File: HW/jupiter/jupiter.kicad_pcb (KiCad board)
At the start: 2 copper layers, 32 parts, among them J1 POWER_IN, J2 Expansion Bus, Q1 DS1813, SW1 RESET, SW2 PANIC, SW3 SPDT, U1 TL7705B, U2 74HC74, U3 DS1511Y+, U4 WD65C816S_PLCC44-65xx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

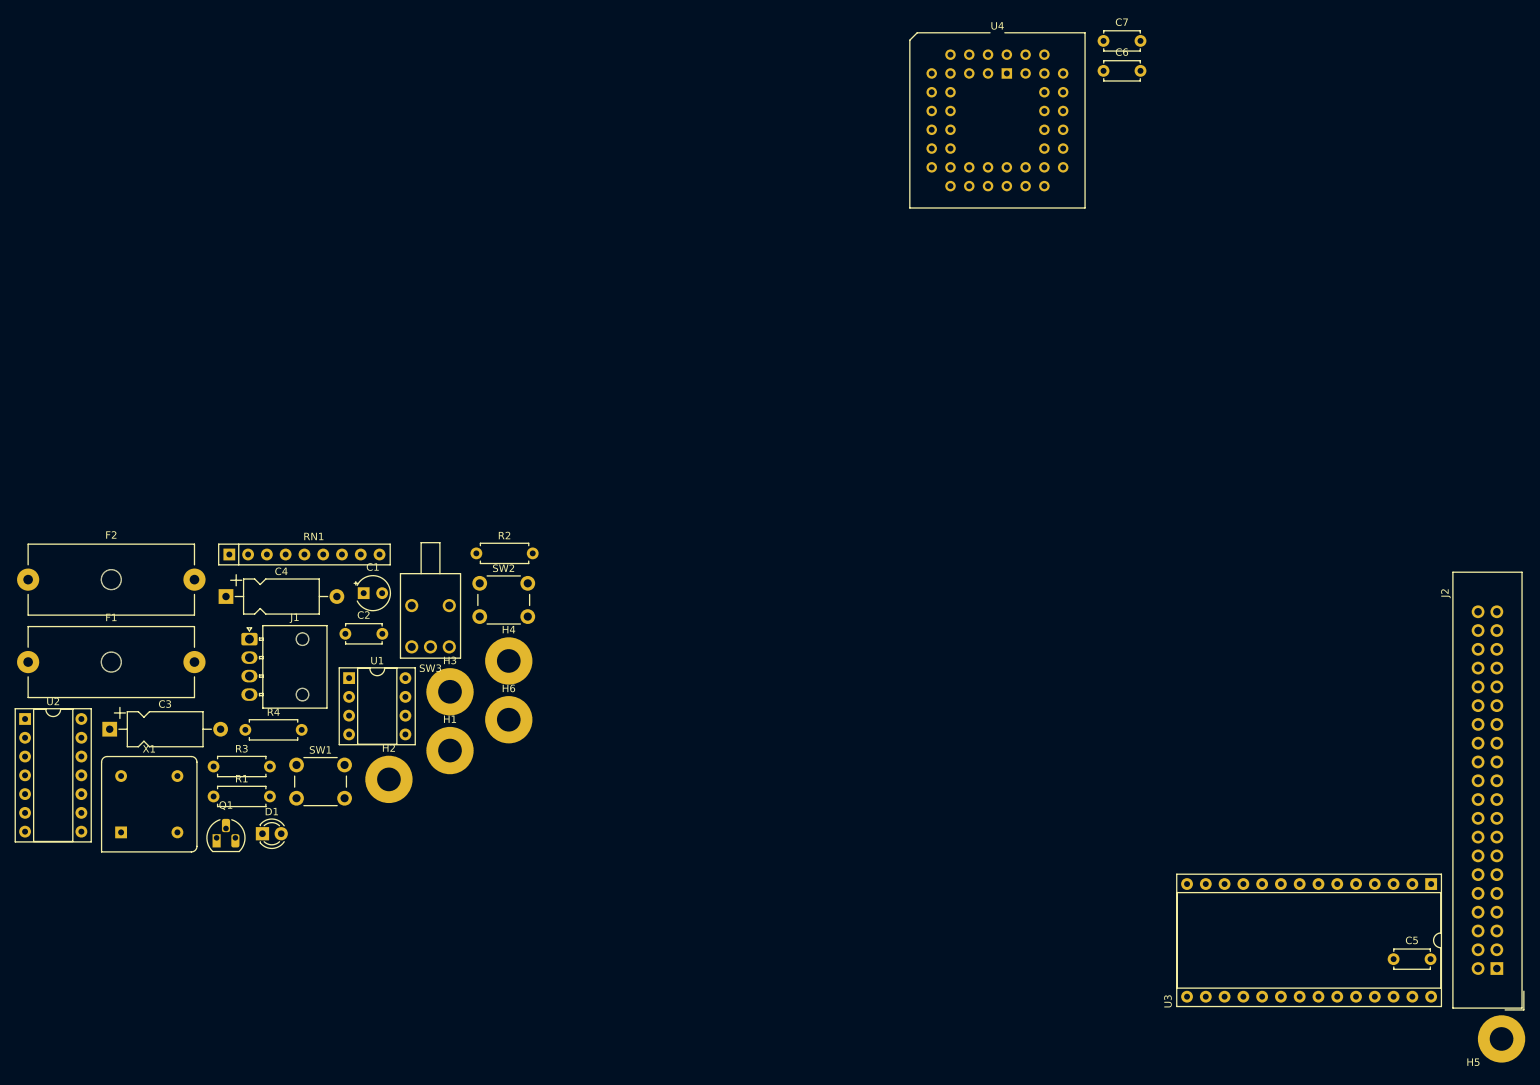
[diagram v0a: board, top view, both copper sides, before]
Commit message: Added PCB train technical capabilities.
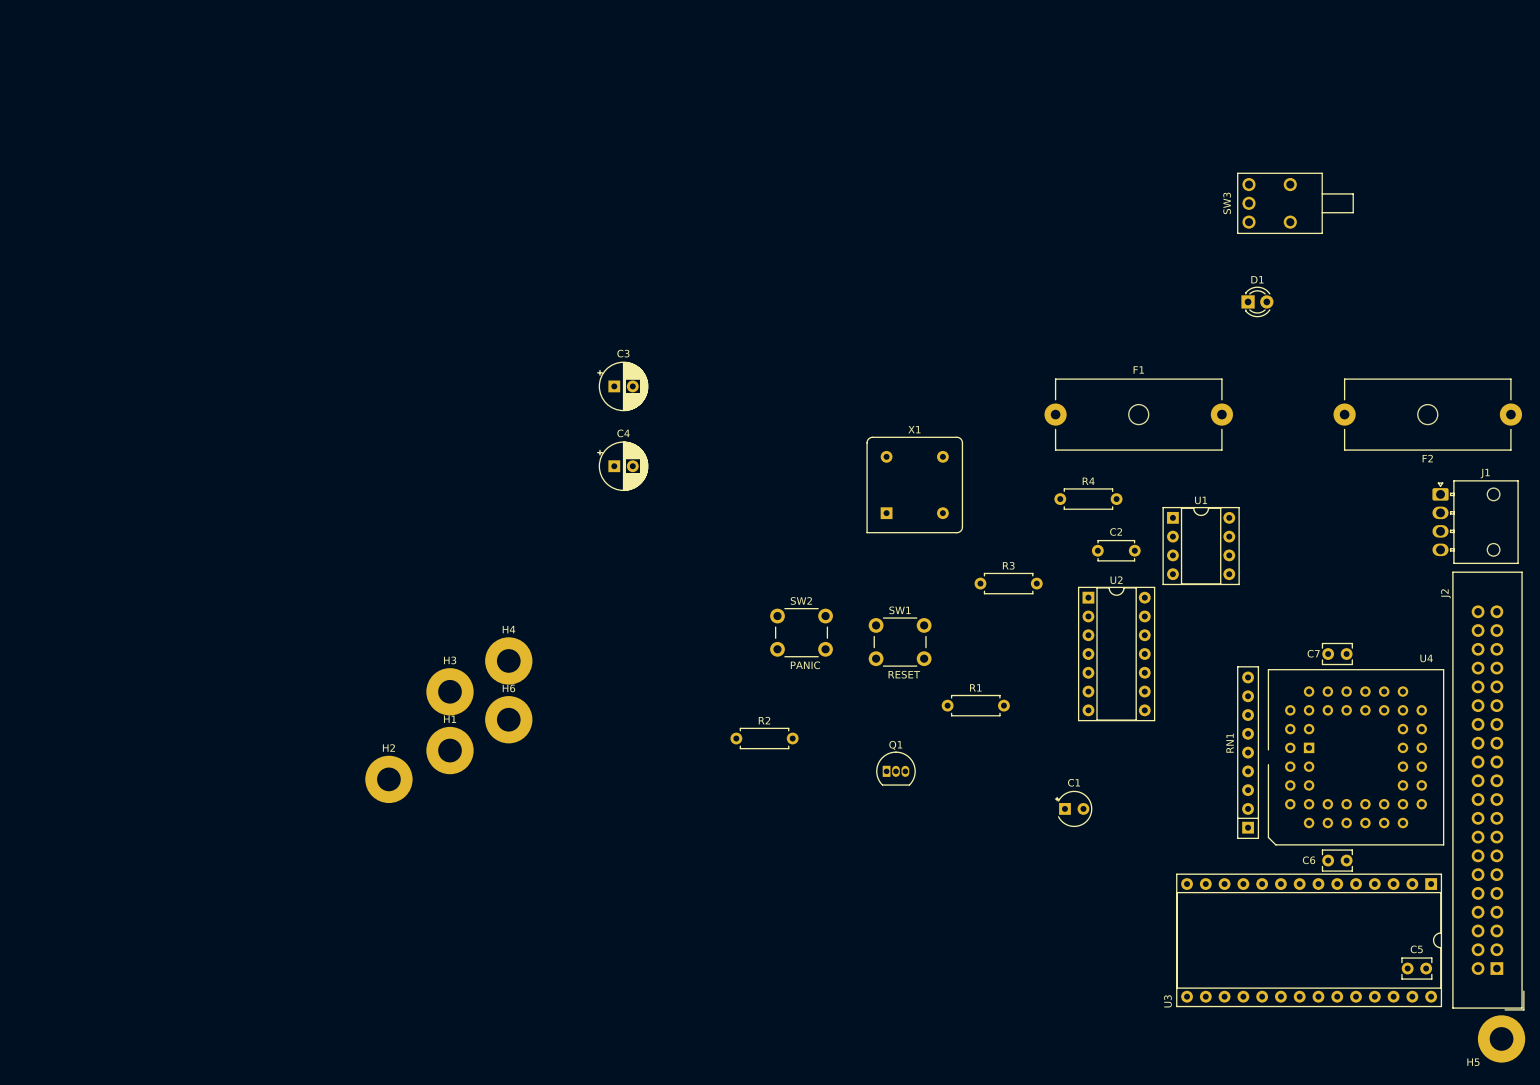
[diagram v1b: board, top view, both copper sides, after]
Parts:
- C3, C4: footprint Capacitor_THT:CP_Axial_L10.0mm_D4.5mm_P15.00mm_Horizontal -> Capacitor_THT:CP_Radial_D6.3mm_P2.50mm
- C5, C6, C7: footprint Capacitor_THT:C_Disc_D4.7mm_W2.5mm_P5.00mm -> Capacitor_THT:C_Disc_D3.8mm_W2.6mm_P2.50mm
- Q1: footprint Package_TO_SOT_THT:TO-92_HandSolder -> Package_TO_SOT_THT:TO-92_Inline
- moved F2 201.8 mm to (230.5, 69.8), turned to 180 degrees
- moved J1 162.3 mm to (221.0, 80.6)
- moved D1 151.5 mm to (194.9, 54.6)
- moved U2 144.8 mm to (173.4, 94.6)
- moved F1 143.0 mm to (168.9, 69.8)
- moved RN1 142.7 mm to (194.9, 125.7), turned to 90 degrees
- moved SW3 127.2 mm to (198.1, 41.3), turned to 270 degrees
- moved R4 114.6 mm to (169.5, 81.3)
- moved U1 113.5 mm to (184.8, 83.8)
- moved X1 112.2 mm to (146.1, 83.2)
- moved C6 111.1 mm to (205.8, 130.2)
- moved R3 106.6 mm to (158.8, 92.7)
- moved C2 102.4 mm to (174.6, 88.3)
- moved R1 100.0 mm to (154.3, 109.2)
- moved U4 100.0 mm to (203.2, 114.9), turned to 90 degrees
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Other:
- copper layers 2 -> 4
- net class Default: clearance 0.2 -> 0.15; trace_width 0.25 -> 0.15; via_dia 0.8 -> 0.5; via_drill 0.4 -> 0.3
- net class GND added: clearance 0.15, trace_width 0.15, via_dia 0.5, via_drill 0.3
- net class PWR_IN added: clearance 0.5, trace_width 1, via_dia 0.5, via_drill 0.3
- net class VCC added: clearance 0.15, trace_width 0.15, via_dia 0.5, via_drill 0.3
- rule trace_clearance: 0.2 -> 0.15
- rule trace_min: 0.2 -> 0.125

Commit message: started to layout the pcb.
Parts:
- moved SW1 68.1 mm to (212.7, 98.4), turned to 180 degrees
- moved R2 67.3 mm to (191.8, 101.0), turned to 270 degrees
- moved R3 58.5 mm to (216.5, 101.6), turned to 90 degrees
- moved R1 49.9 mm to (200.7, 90.8)
- moved C1 24.1 mm to (191.8, 112.4), turned to 180 degrees
- moved C2 17.9 mm to (191.8, 93.4), turned to 270 degrees
- moved U1 14.4 mm to (194.9, 94.0)
